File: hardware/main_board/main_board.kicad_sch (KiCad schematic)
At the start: 49 parts, among them J1 rgb 0, J10 uart, J11 input 4, J12 input 5, J13 rgb 3, J14 +5v out, J15 rgb 4, J16 input 6, J17 input 7, J18 rgb 5, J19 rgb output, J2 +12v 3a in, J20 ypbpr output, J21 rgb 6, J22 rgb 7, J3 input 0, J4 input 1, J5 icsp, J6 rgb 1, J7 input 2, J8 input 3, J9 rgb 2, SW10 prev, SW11 next, SW12 csync/rgbs, SW13 csync/rgbs, SW14 csync/rgbs, SW15 csync/rgbs, SW16 csync/rgbs, SW17 csync/rgbs, SW18 csync/rgbs, SW19 csync/rgbs, SW20 csync/rgbs, SW9 on/off, U1 ATmega328PB-A, U2 L7805

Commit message: #5: Removed LED-related things from main_board. Replaced power inlet with USB-C connector configured to accept 5V. Not sure what current consumption will be like though...
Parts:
- removed C5: 100n, Capacitor_SMD:C_0603_1608Metric, symbol Device:C_Small
- removed C6: 100u, Capacitor_SMD:CP_Elec_6.3x7.7, symbol Device:C_Polarized_Small
- removed D1: power, LED_SMD:LED_0603_1608Metric, symbol Device:LED_Small
- removed J1: rgb 0, Connector_Phoenix_MC:PhoenixContact_MC_1,5_4-G-3.5_1x04_P3.50mm_Horizontal, symbol Connector_Generic:Conn_01x04
- removed J13: rgb 3, Connector_Phoenix_MC:PhoenixContact_MC_1,5_4-G-3.5_1x04_P3.50mm_Horizontal, symbol Connector_Generic:Conn_01x04
- removed J15: rgb 4, Connector_Phoenix_MC:PhoenixContact_MC_1,5_4-G-3.5_1x04_P3.50mm_Horizontal, symbol Connector_Generic:Conn_01x04
- removed J18: rgb 5, Connector_Phoenix_MC:PhoenixContact_MC_1,5_4-G-3.5_1x04_P3.50mm_Horizontal, symbol Connector_Generic:Conn_01x04
- removed J2: +12v 3a in, Connector_BarrelJack:BarrelJack_CLIFF_FC681465S_SMT_Horizontal, symbol Connector:Barrel_Jack_Switch
- removed J21: rgb 6, Connector_Phoenix_MC:PhoenixContact_MC_1,5_4-G-3.5_1x04_P3.50mm_Horizontal, symbol Connector_Generic:Conn_01x04
- removed J22: rgb 7, Connector_Phoenix_MC:PhoenixContact_MC_1,5_4-G-3.5_1x04_P3.50mm_Horizontal, symbol Connector_Generic:Conn_01x04
- removed J6: rgb 1, Connector_Phoenix_MC:PhoenixContact_MC_1,5_4-G-3.5_1x04_P3.50mm_Horizontal, symbol Connector_Generic:Conn_01x04
- removed J9: rgb 2, Connector_Phoenix_MC:PhoenixContact_MC_1,5_4-G-3.5_1x04_P3.50mm_Horizontal, symbol Connector_Generic:Conn_01x04
- removed SW9: on/off, MTS-102:SW_Toggle_Blue_wSlots, symbol Switch:SW_SPDT
- removed U2: L7805, Package_TO_SOT_SMD:TO-263-2, symbol Regulator_Linear:L7805
- added J1: +5v in, symbol Connector:USB_C_Receptacle_PowerOnly_6P
- added R2: 5k1, Resistor_SMD:R_0603_1608Metric, symbol Device:R_Small
- C3: value 10u -> 100n
- C4: value 100n -> 10u
- R3: value 6k8 -> 5k1
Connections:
- net +5V: now also J1.A9 (VBUS), J1.B9 (VBUS)
- net GND: now also J1.A12 (GND), J1.B12 (GND), J1.S1 (SHIELD), R2.2
- net at R3.1: now also J1.B5 (CC2)
- net PIN_LEDB: no longer names the net of U1.1 (PD3)
- net PIN_LEDG: no longer names the net of U1.9 (PD5)
- net PIN_LEDR: no longer names the net of U1.10 (PD6)
- new net: J1.A5 (CC1), R2.1
- no-connect marks 34 -> 37
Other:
- removed sheet led switching
- note added: "SAMZO UKDBBTAAA"
- note added: "i'm deliberately not putting +5v on this connector so we can plug FTDI <-> 3.5mm cables straight into this."
- note removed: "MTS-102 or equivalent, 4.7mm pitch"
- note removed: "Phoenix Contact MC 1,5/4-G-3,5"
- note removed: "XKB DC-005-5A-2.5-SMT"
- note removed: "i'm deliberately not putting +5v on a single connector so we can plug FTDI <-> 3.5mm cables straight into this."
- note removed: "rgb led strips"

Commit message: #5: Got the PCB layout into a relatively clean state before I play with the layout and size.
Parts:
- J1: footprint (none) -> Connector_USB:USB_C_Receptacle_HRO_TYPE-C-31-M-17
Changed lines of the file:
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@@
 			)
 		)
-		(property "Footprint" ""
+		(property "Footprint" "Connector_USB:USB_C_Receptacle_HRO_TYPE-C-31-M-17"
 			(at 38.1 46.99 0)
 			(effects

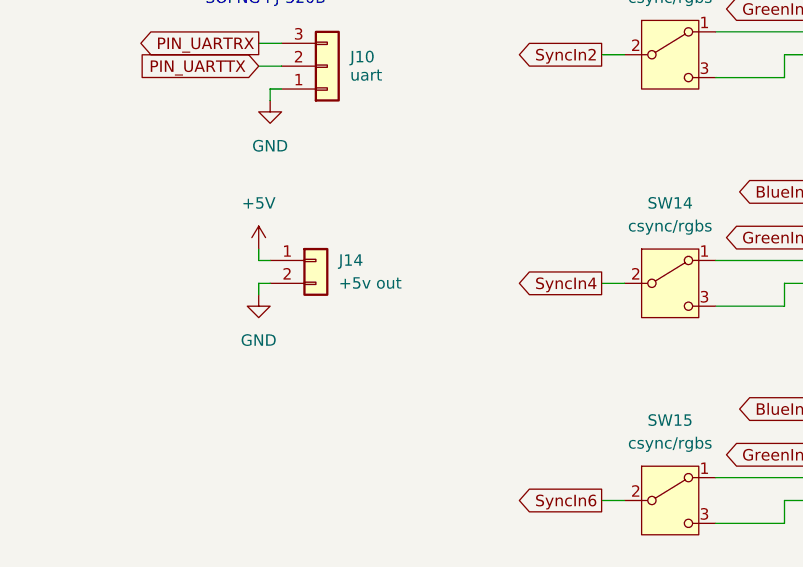
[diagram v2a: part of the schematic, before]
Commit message: #5: Fix missing C19. Minor artwork updates. Actually, why not let the +5v connector be in/out?
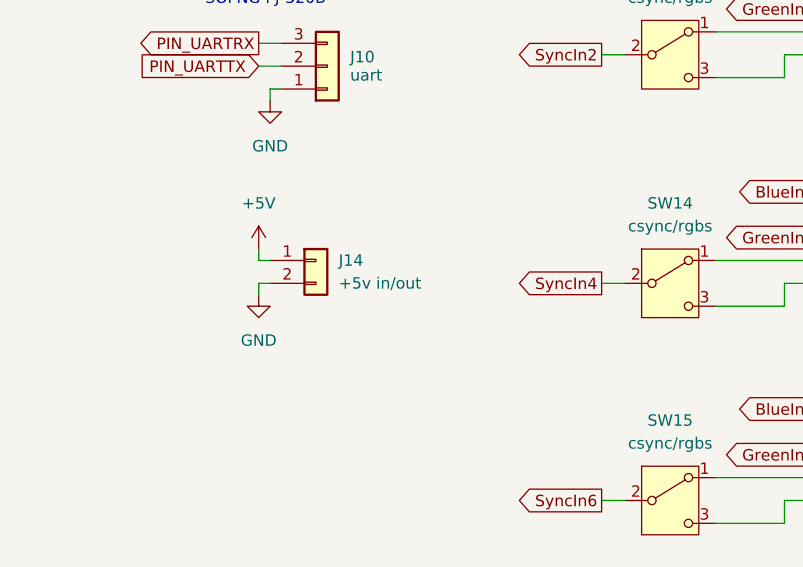
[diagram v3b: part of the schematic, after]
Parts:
- J14: value +5v out -> +5v in/out
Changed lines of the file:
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@@
 			)
 		)
-		(property "Value" "+5v out"
+		(property "Value" "+5v in/out"
 			(at 53.34 125.7299 0)
 			(effects

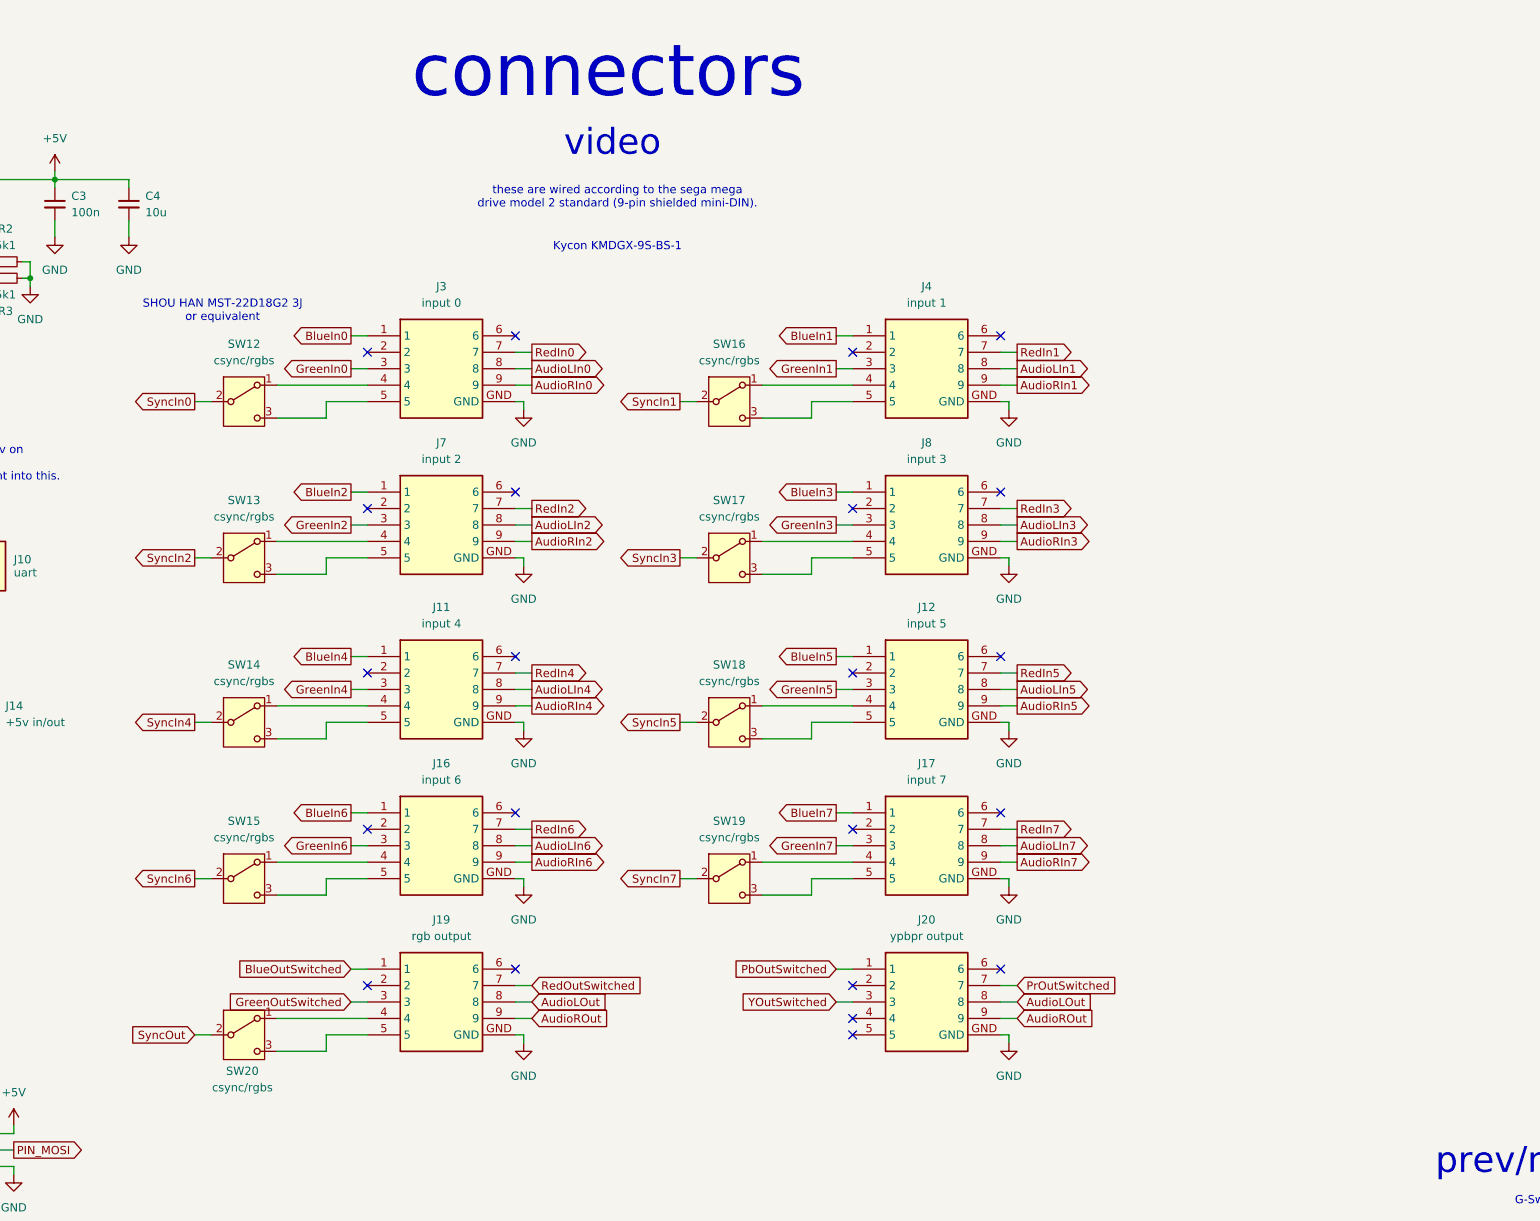
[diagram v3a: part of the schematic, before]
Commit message: #5: Properly handle unused NOT gate. Prune unused symbol/footprint libs.
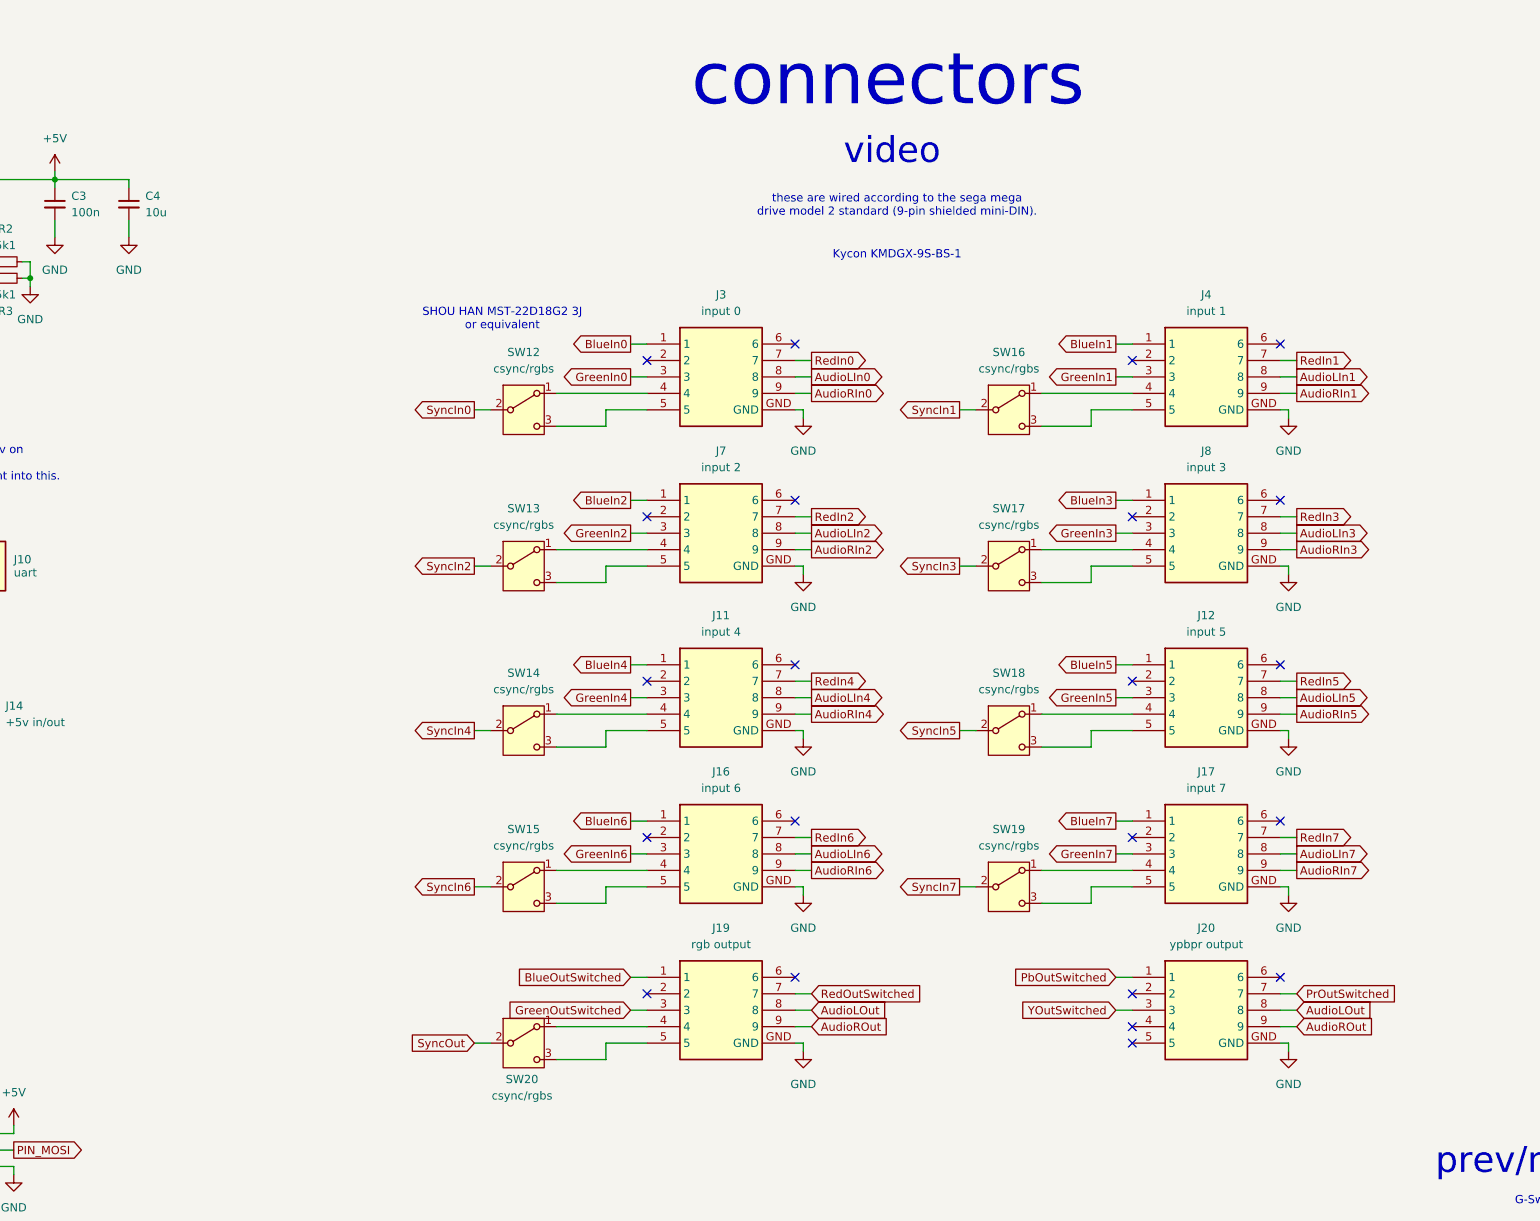
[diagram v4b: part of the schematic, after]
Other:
- moved on the sheet: J11, J12, J16, J17, J19, J20, J3, J4, J7, J8, SW12, SW13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

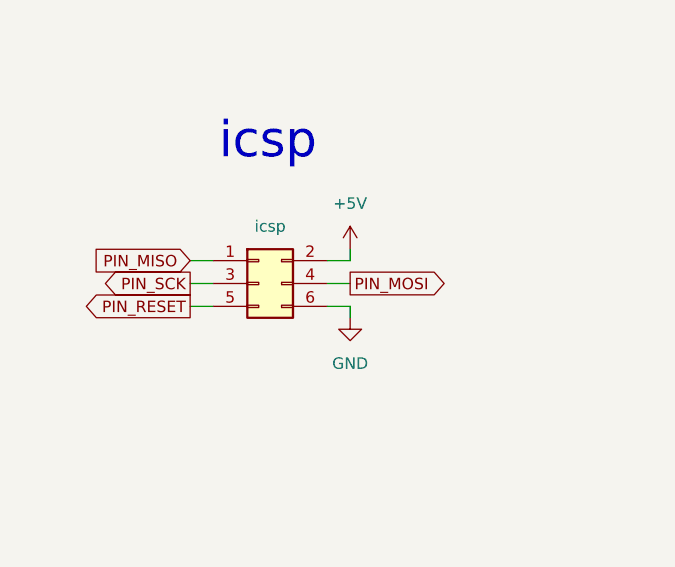
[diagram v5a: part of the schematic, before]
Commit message: #5: Started LED board project. More README.md updates. Move MTS-102 footprint to LED board.
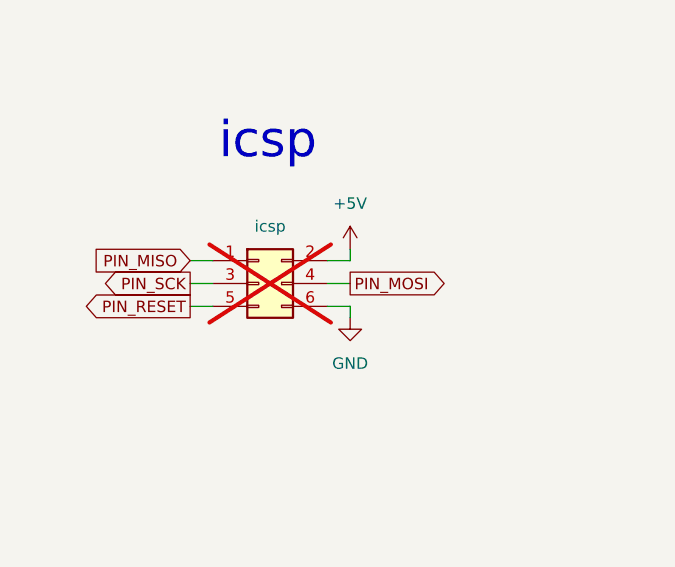
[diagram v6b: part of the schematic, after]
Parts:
- J5: now not fitted; now left out of the parts list
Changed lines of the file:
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@@
 		(unit 1)
 		(exclude_from_sim no)
-		(in_bom yes)
+		(in_bom no)
 		(on_board yes)
-		(dnp no)
+		(dnp yes)
 		(fields_autoplaced yes)
 		(property "Reference" "J5"

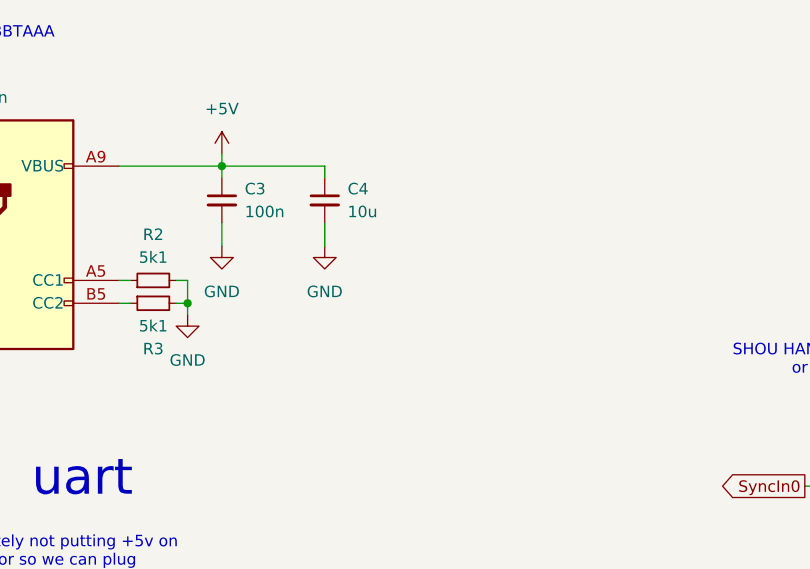
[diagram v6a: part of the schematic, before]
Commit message: #5: Fixed dumb mistake I made where I got rid of the power LED!
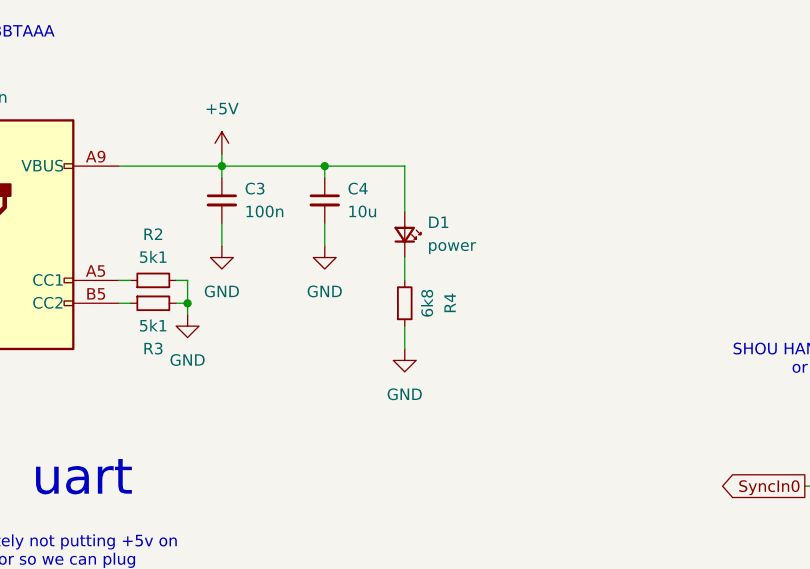
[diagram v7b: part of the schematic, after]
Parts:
- added D1: power, LED_SMD:LED_0603_1608Metric, symbol Device:LED_Small
- added R4: 6k8, Resistor_SMD:R_0603_1608Metric, symbol Device:R_Small
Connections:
- net +5V: now also D1.2 (A)
- net GND: now also R4.1
- new net: D1.1 (K), R4.2
